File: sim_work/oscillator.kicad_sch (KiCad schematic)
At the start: 26 parts, among them U1 LM4562, U2 LM4562, U3 LM4562

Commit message: Oscillator schematic fixes, SimGUI verification, pipeline improvement plan
- Fix diode orientation (rotation 90/270 → 0/180) for correct pin-to-wire connectivity
- Fix feedback/VEE wire overlap that shorted -15V to inverting inputs
- Fix SPI0_CLK/VCTRL net collision (label → text annotation)
- Reduce feedback height above op-amps (fb_vert 14→6, damp_vert 22→10)
- Scale stroke widths in scale_schematic() for visibility at 3x
- Increase left margin (c1x 10→15) to prevent title clipping
- Add multi-point oscillator simulation results (D=12,60,605,1211,2421)
- Rewrite README with full project description and resource table
- Update PROJECT.md with Session 16-17 fixes and pipeline improvement roadmap

Co-Authored-By: Claude Opus 4.6 <noreply@anthropic.com>
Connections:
- net -15V: no longer C1.1, C2.1, R4.2, R5.1, R6.2, R7.1, U2.2 (-), U3.2 (-)
- net BP: now also C1.1, D1.1 (K), D1.2 (A), D2.1 (K), D2.2 (A), R4.2, R5.1, U2.2 (-)
- net LP: now also C2.1, D3.1 (K), D3.2 (A), D4.1 (K), D4.2 (A), R6.2, R7.1, U3.2 (-)
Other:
- note added: "1/5 attenuator Vin/5 to AD636"
- note added: "SPI0 -> DAC7800 controls VCTRL"
- note added: "STARTUP KICK + POWER SUPPLY"
- note added: "Startup Kick PULSE 0.1V 10us"
- note removed: "1/5 atten Vin/5 to AD636"
- note removed: "3.3V"
- note removed: "DAC_CS"
- note removed: "POWER SUPPLY"
- note removed: "PULSE 0.1V 10us"
- note removed: "SPI0 -> DAC7800 controls frequency"
- note removed: "SPI0_CLK"
- note removed: "SPI0_MOSI"
- note removed: "Startup Kick"
- note removed: "UART_TX"
- company: CircuitForge -> CircuitForge - Bob Smith

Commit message: Verification system overhaul + professional schematic layout
- Dynamic pin parser reads 22,607 KiCad symbol libraries for ALL component types
- Wire overlap detection catches collinear segments sharing ranges
- Wire merge post-processing auto-deduplicates overlapping wires
- simulate() now fails on non-zero exit codes, snapshots stale files
- Switched to 1x scale on standard A3/A4 paper (was 3x on custom paper)
- Section titles repositioned above components, MCU block boxed
- Clearance parameters added as kwargs for correction loop tuning

Oscillator: A3 1:1, 97% fill, 0 errors, 0 wire overlaps
TIA: A4 1:1, 96% fill, 0 errors, 0 wire overlaps

Co-Authored-By: Claude Opus 4.6 <noreply@anthropic.com>
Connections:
- net BP: no longer C1.1, D1.1 (K), D1.2 (A), D2.1 (K), D2.2 (A), R4.2, R5.1, U2.2 (-)
- net LP: no longer C2.1, D3.1 (K), D3.2 (A), D4.1 (K), D4.2 (A), R6.2, R7.1, U3.2 (-)
- net at R1.2, R2.2, U1.2 (-): no longer R3.1
- new net: D1.1 (K), D2.1 (K)
- new net: C1.1, R4.2, R5.1
- new net: C2.1, R6.2, R7.1
- new net: D3.1 (K), D4.1 (K)

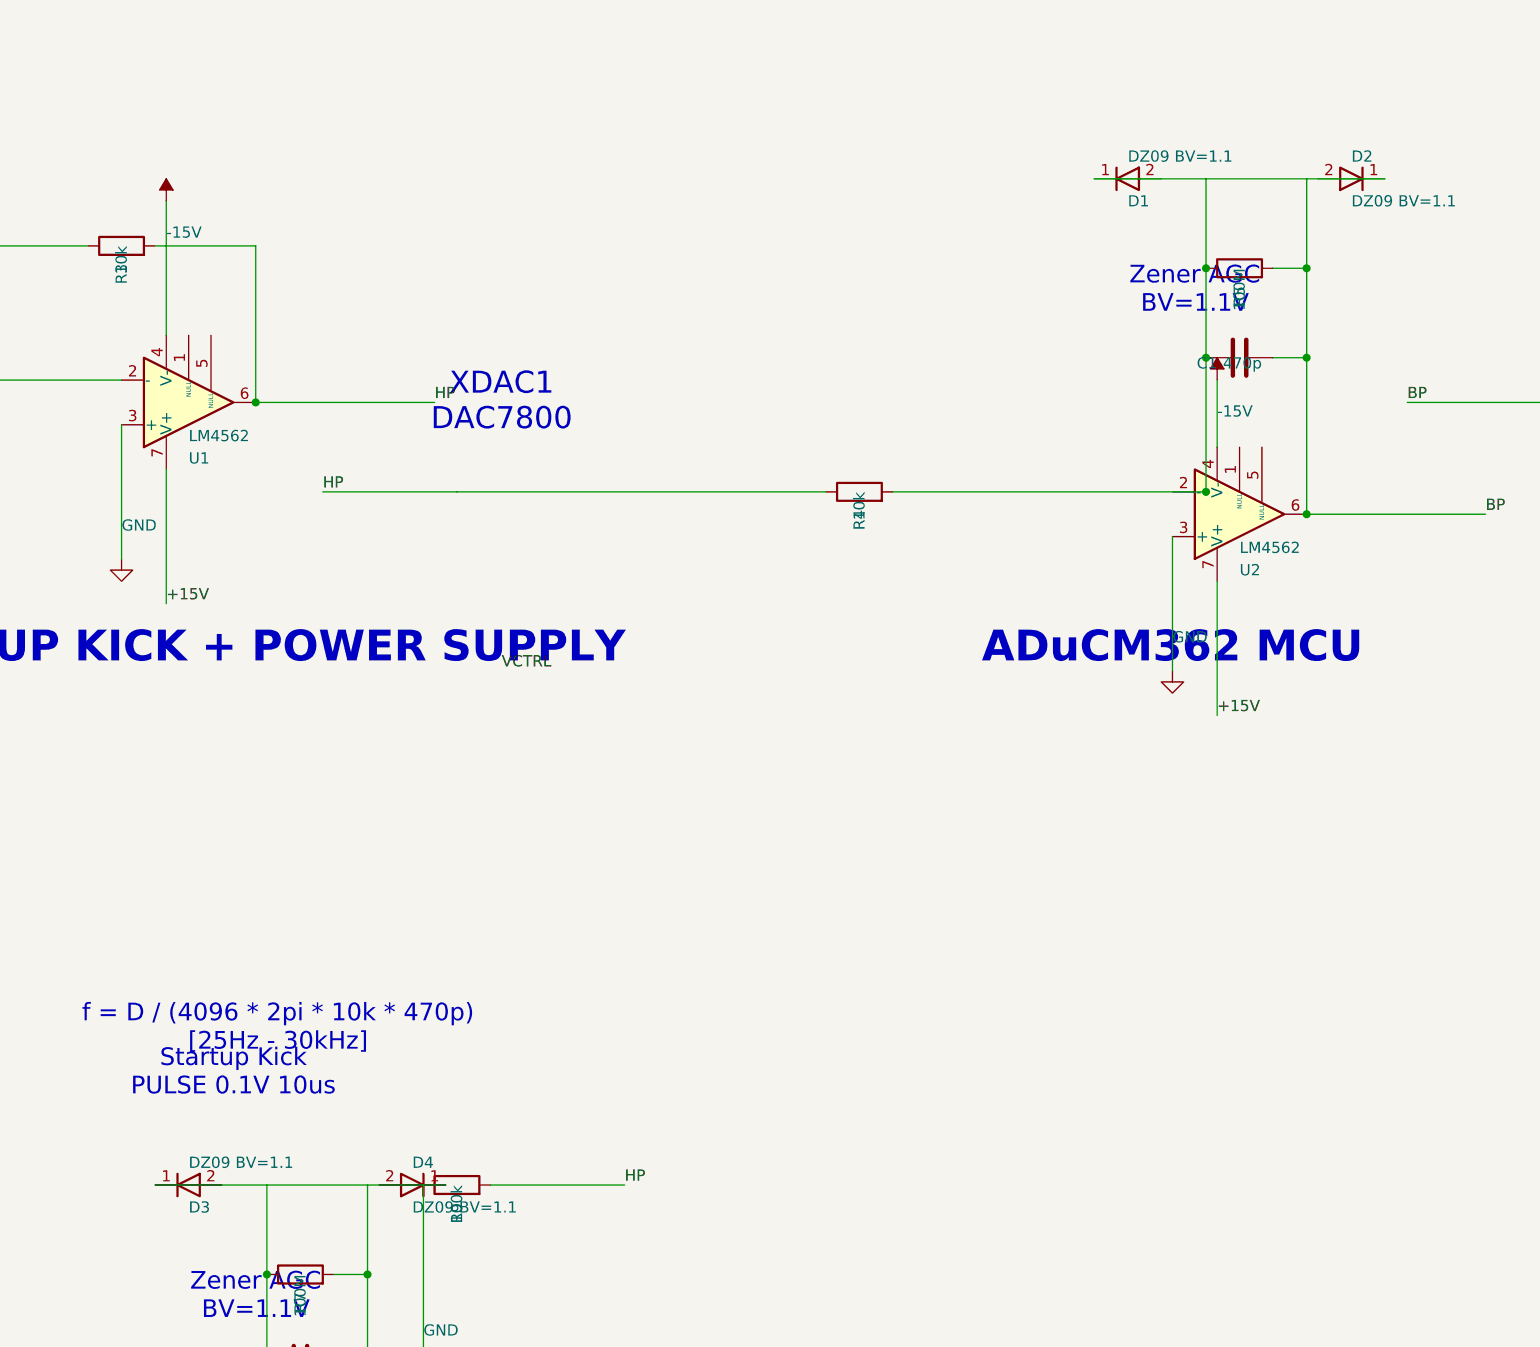
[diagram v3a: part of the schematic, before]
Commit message: Fix schematic connections, add docs and repo portability
- Input filters: R rotation=90 (horizontal), ESD diode rotations fixed,
  junction dots at cathode-signal connection, wires to GND symbols
- Relay ladder: flyback diode rotation 270->90 (K top, A bottom)
- Electrometer/Mux TIA: 4 junction dots each at T-junctions
- AD636 RMS detector: proper IC box with pin labels replaces text-only
- Oscillator blocks: D_Zener symbol, L-shaped cathode routing
- TIA blocks: title/function annotations on all 5 blocks
- New: requirements.txt, docs/oscillator_guide.md
- D_Zener.kicad_sym added to bundled symbols/
- .gitignore updated for docs/ and requirements.txt
- README updated with pip install -r requirements.txt
- PROJECT.md session 9 changelog
- SimGUI builds clean (0 errors)

Co-Authored-By: Claude Opus 4.6 <noreply@anthropic.com>
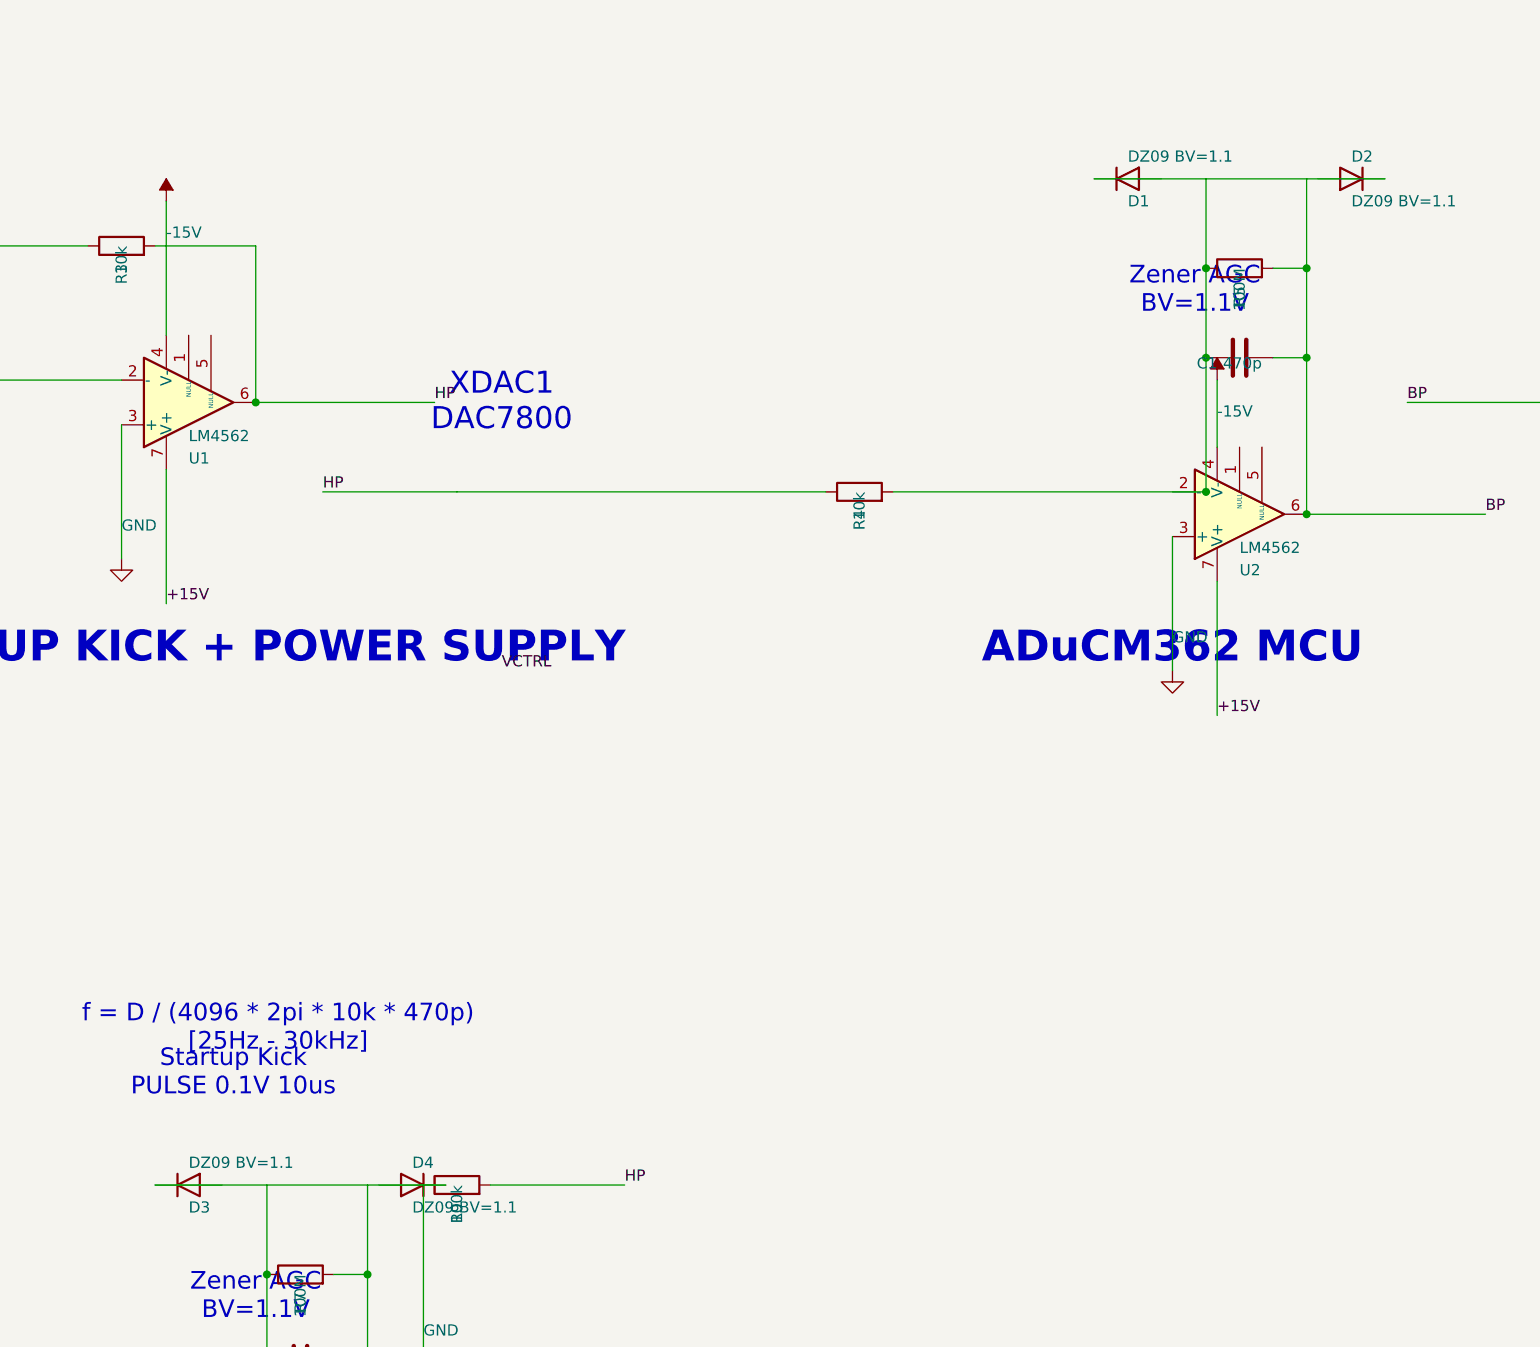
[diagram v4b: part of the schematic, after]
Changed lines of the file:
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@@
 		(instances
 			(project "State Variable Oscillator with MDAC Control"
-				(path "/075f6cc2-500d-4818-87f7-12acd1047ab1"
+				(path "/de47d635-bb16-490a-9463-fbb7ddc35300"
 					(reference "U1")
 					(unit 1)
@@
 		(instances
 			(project "State Variable Oscillator with MDAC Control"
-				(path "/075f6cc2-500d-4818-87f7-12acd1047ab1"
+				(path "/de47d635-bb16-490a-9463-fbb7ddc35300"
 					(reference "R1")
 					(unit 1)
@@
 		(instances
 			(project "State Variable Oscillator with MDAC Control"
-				(path "/075f6cc2-500d-4818-87f7-12acd1047ab1"
+				(path "/de47d635-bb16-490a-9463-fbb7ddc35300"
 					(reference "R2")
 					(unit 1)
@@
 		(instances
 			(project "State Variable Oscillator with MDAC Control"
-				(path "/075f6cc2-500d-4818-87f7-12acd1047ab1"
+				(path "/de47d635-bb16-490a-9463-fbb7ddc35300"
 					(reference "R3")
 					(unit 1)
@@
 		(instances
 			(project "State Variable Oscillator with MDAC Control"
-				(path "/075f6cc2-500d-4818-87f7-12acd1047ab1"
+				(path "/de47d635-bb16-490a-9463-fbb7ddc35300"
 					(reference "#PWR001")
 					(unit 1)
@@
 		(instances
 			(project "State Variable Oscillator with MDAC Control"
-				(path "/075f6cc2-500d-4818-87f7-12acd1047ab1"
+				(path "/de47d635-bb16-490a-9463-fbb7ddc35300"
 					(reference "#PWR002")
 					(unit 1)
@@
 		(instances
 			(project "State Variable Oscillator with MDAC Control"
-				(path "/075f6cc2-500d-4818-87f7-12acd1047ab1"
+				(path "/de47d635-bb16-490a-9463-fbb7ddc35300"
 					(reference "U2")
 					(unit 1)
@@
 		(instances
 			(project "State Variable Oscillator with MDAC Control"
-				(path "/075f6cc2-500d-4818-87f7-12acd1047ab1"
+				(path "/de47d635-bb16-490a-9463-fbb7ddc35300"
 					(reference "R4")
 					(unit 1)
@@
 		(instances
 			(project "State Variable Oscillator with MDAC Control"
-				(path "/075f6cc2-500d-4818-87f7-12acd1047ab1"
+				(path "/de47d635-bb16-490a-9463-fbb7ddc35300"
 					(reference "C1")
 					(unit 1)
@@
 		(instances
 			(project "State Variable Oscillator with MDAC Control"
-				(path "/075f6cc2-500d-4818-87f7-12acd1047ab1"
+				(path "/de47d635-bb16-490a-9463-fbb7ddc35300"
 					(reference "R5")
 					(unit 1)
@@
 		(instances
 			(project "State Variable Oscillator with MDAC Control"
-				(path "/075f6cc2-500d-4818-87f7-12acd1047ab1"
+				(path "/de47d635-bb16-490a-9463-fbb7ddc35300"
 					(reference "D1")
 					(unit 1)
@@
 		(instances
 			(project "State Variable Oscillator with MDAC Control"
-				(path "/075f6cc2-500d-4818-87f7-12acd1047ab1"
+				(path "/de47d635-bb16-490a-9463-fbb7ddc35300"
 					(reference "D2")
 					(unit 1)
@@
 		(instances
 			(project "State Variable Oscillator with MDAC Control"
-				(path "/075f6cc2-500d-4818-87f7-12acd1047ab1"
+				(path "/de47d635-bb16-490a-9463-fbb7ddc35300"
 					(reference "#PWR003")
 					(unit 1)
@@
 		(instances
 			(project "State Variable Oscillator with MDAC Control"
-				(path "/075f6cc2-500d-4818-87f7-12acd1047ab1"
+				(path "/de47d635-bb16-490a-9463-fbb7ddc35300"
 					(reference "#PWR004")
 					(unit 1)
@@
 		(instances
 			(project "State Variable Oscillator with MDAC Control"
-				(path "/075f6cc2-500d-4818-87f7-12acd1047ab1"
+				(path "/de47d635-bb16-490a-9463-fbb7ddc35300"
 					(reference "R10")
 					(unit 1)
@@
 		(instances
 			(project "State Variable Oscillator with MDAC Control"
-				(path "/075f6cc2-500d-4818-87f7-12acd1047ab1"
+				(path "/de47d635-bb16-490a-9463-fbb7ddc35300"
 					(reference "R11")
 					(unit 1)
@@
 		(instances
 			(project "State Variable Oscillator with MDAC Control"
-				(path "/075f6cc2-500d-4818-87f7-12acd1047ab1"
+				(path "/de47d635-bb16-490a-9463-fbb7ddc35300"
 					(reference "#PWR005")
 					(unit 1)
@@
 		(instances
 			(project "State Variable Oscillator with MDAC Control"
-				(path "/075f6cc2-500d-4818-87f7-12acd1047ab1"
+				(path "/de47d635-bb16-490a-9463-fbb7ddc35300"
 					(reference "C3")
 					(unit 1)
@@
 		(instances
 			(project "State Variable Oscillator with MDAC Control"
-				(path "/075f6cc2-500d-4818-87f7-12acd1047ab1"
+				(path "/de47d635-bb16-490a-9463-fbb7ddc35300"
 					(reference "#PWR006")
 					(unit 1)
@@
 		(instances
 			(project "State Variable Oscillator with MDAC Control"
-				(path "/075f6cc2-500d-4818-87f7-12acd1047ab1"
+				(path "/de47d635-bb16-490a-9463-fbb7ddc35300"
 					(reference "U3")
 					(unit 1)
@@
 		(instances
 			(project "State Variable Oscillator with MDAC Control"
-				(path "/075f6cc2-500d-4818-87f7-12acd1047ab1"
+				(path "/de47d635-bb16-490a-9463-fbb7ddc35300"
 					(reference "R6")
 					(unit 1)
@@
 		(instances
 			(project "State Variable Oscillator with MDAC Control"
-				(path "/075f6cc2-500d-4818-87f7-12acd1047ab1"
+				(path "/de47d635-bb16-490a-9463-fbb7ddc35300"
 					(reference "C2")
 					(unit 1)
@@
 		(instances
 			(project "State Variable Oscillator with MDAC Control"
-				(path "/075f6cc2-500d-4818-87f7-12acd1047ab1"
+				(path "/de47d635-bb16-490a-9463-fbb7ddc35300"
 					(reference "R7")
 					(unit 1)
@@
 		(instances
 			(project "State Variable Oscillator with MDAC Control"
-				(path "/075f6cc2-500d-4818-87f7-12acd1047ab1"
+				(path "/de47d635-bb16-490a-9463-fbb7ddc35300"
 					(reference "D3")
 					(unit 1)
@@
 		(instances
 			(project "State Variable Oscillator with MDAC Control"
-				(path "/075f6cc2-500d-4818-87f7-12acd1047ab1"
+				(path "/de47d635-bb16-490a-9463-fbb7ddc35300"
 					(reference "D4")
 					(unit 1)
@@
 		(instances
 			(project "State Variable Oscillator with MDAC Control"
-				(path "/075f6cc2-500d-4818-87f7-12acd1047ab1"
+				(path "/de47d635-bb16-490a-9463-fbb7ddc35300"
 					(reference "#PWR007")
 					(unit 1)
@@
 		(instances
 			(project "State Variable Oscillator with MDAC Control"
-				(path "/075f6cc2-500d-4818-87f7-12acd1047ab1"
+				(path "/de47d635-bb16-490a-9463-fbb7ddc35300"
 					(reference "#PWR008")
 					(unit 1)
@@
 		(instances
 			(project "State Variable Oscillator with MDAC Control"
-				(path "/075f6cc2-500d-4818-87f7-12acd1047ab1"
+				(path "/de47d635-bb16-490a-9463-fbb7ddc35300"
 					(reference "R8")
 					(unit 1)
@@
 		(instances
 			(project "State Variable Oscillator with MDAC Control"
-				(path "/075f6cc2-500d-4818-87f7-12acd1047ab1"
+				(path "/de47d635-bb16-490a-9463-fbb7ddc35300"
 					(reference "#PWR009")
 					(unit 1)
@@
 		(instances
 			(project "State Variable Oscillator with MDAC Control"
-				(path "/075f6cc2-500d-4818-87f7-12acd1047ab1"
+				(path "/de47d635-bb16-490a-9463-fbb7ddc35300"
 					(reference "R9")
 					(unit 1)
@@
 		(instances
 			(project "State Variable Oscillator with MDAC Control"
-				(path "/075f6cc2-500d-4818-87f7-12acd1047ab1"
+				(path "/de47d635-bb16-490a-9463-fbb7ddc35300"
 					(reference "#PWR010")
 					(unit 1)
@@
 		(instances
 			(project "State Variable Oscillator with MDAC Control"
-				(path "/075f6cc2-500d-4818-87f7-12acd1047ab1"
+				(path "/de47d635-bb16-490a-9463-fbb7ddc35300"
 					(reference "C6")
 					(unit 1)
@@
 		(instances
 			(project "State Variable Oscillator with MDAC Control"
-				(path "/075f6cc2-500d-4818-87f7-12acd1047ab1"
+				(path "/de47d635-bb16-490a-9463-fbb7ddc35300"
 					(reference "#PWR011")
 					(unit 1)
@@
 		(instances
 			(project "State Variable Oscillator with MDAC Control"
-				(path "/075f6cc2-500d-4818-87f7-12acd1047ab1"
+				(path "/de47d635-bb16-490a-9463-fbb7ddc35300"
 					(reference "#PWR012")
 					(unit 1)
@@
 		(instances
 			(project "State Variable Oscillator with MDAC Control"
-				(path "/075f6cc2-500d-4818-87f7-12acd1047ab1"
+				(path "/de47d635-bb16-490a-9463-fbb7ddc35300"
 					(reference "C7")
 					(unit 1)
@@
 		(instances
 			(project "State Variable Oscillator with MDAC Control"
-				(path "/075f6cc2-500d-4818-87f7-12acd1047ab1"
+				(path "/de47d635-bb16-490a-9463-fbb7ddc35300"
 					(reference "#PWR013")
 					(unit 1)
@@
 		(instances
 			(project "State Variable Oscillator with MDAC Control"
-				(path "/075f6cc2-500d-4818-87f7-12acd1047ab1"
+				(path "/de47d635-bb16-490a-9463-fbb7ddc35300"
 					(reference "C8")
 					(unit 1)
@@
 		(instances
 			(project "State Variable Oscillator with MDAC Control"
-				(path "/075f6cc2-500d-4818-87f7-12acd1047ab1"
+				(path "/de47d635-bb16-490a-9463-fbb7ddc35300"
 					(reference "#PWR014")
 					(unit 1)
@@
 		(instances
 			(project "State Variable Oscillator with MDAC Control"
-				(path "/075f6cc2-500d-4818-87f7-12acd1047ab1"
+				(path "/de47d635-bb16-490a-9463-fbb7ddc35300"
 					(reference "#PWR015")
 					(unit 1)
@@
 		(instances
 			(project "State Variable Oscillator with MDAC Control"
-				(path "/075f6cc2-500d-4818-87f7-12acd1047ab1"
+				(path "/de47d635-bb16-490a-9463-fbb7ddc35300"
 					(reference "C4")
 					(unit 1)
@@
 		(instances
 			(project "State Variable Oscillator with MDAC Control"
-				(path "/075f6cc2-500d-4818-87f7-12acd1047ab1"
+				(path "/de47d635-bb16-490a-9463-fbb7ddc35300"
 					(reference "#PWR016")
 					(unit 1)
@@
 		(instances
 			(project "State Variable Oscillator with MDAC Control"
-				(path "/075f6cc2-500d-4818-87f7-12acd1047ab1"
+				(path "/de47d635-bb16-490a-9463-fbb7ddc35300"
 					(reference "C5")
 					(unit 1)
@@
 		(instances
 			(project "State Variable Oscillator with MDAC Control"
-				(path "/075f6cc2-500d-4818-87f7-12acd1047ab1"
+				(path "/de47d635-bb16-490a-9463-fbb7ddc35300"
 					(reference "#PWR017")
 					(unit 1)

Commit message: Add comparison mode, fix SimGUI subprocess popups, DAC7800 IC boxes
- SimGUI: fix Python path detection (FindPython searches Python312/313/311)
- SimGUI: suppress console popup windows (CREATE_NO_WINDOW for subprocess)
- SimGUI: add Comparison project (MDAC vs Analog oscillator side-by-side)
- SimGUI: fix async wrapping (direct await instead of Task.Run)
- Pipeline: draw DAC7800 as proper IC box with pin labels (VREF/IOUT/VCTRL)
- Pipeline: fix electrometer_362 layout (spacing, junction dots at T-junctions)
- Pipeline: fix summing amp gain annotations (BP=-0.455, not -2.2)
- Pipeline: add analog_osc command for friend's SVF oscillator simulation
- Docs: comparison_guide.md, updated README and PROJECT tracker

Co-Authored-By: Claude Opus 4.6 <noreply@anthropic.com>
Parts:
- removed D1, D2, D3, D4: DZ09 BV=1.1, symbol D:D
- added D1, D2, D3, D4: DZ09 BV=1.1, symbol D_Zener:D_Zener
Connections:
- net +15V: now also U1.4 (V-), U2.4 (V-), U3.4 (V-); no longer U1.7 (V+), U2.7 (V+), U3.7 (V+)
- net -15V: now also U1.7 (V+), U2.7 (V+), U3.7 (V+); no longer U1.4 (V-), U2.4 (V-), U3.4 (V-)
- net BP: now also D2.1 (K); no longer R6.1
- net GND: now also U1.2 (-), U2.2 (-), U3.2 (-); no longer U1.3 (+), U2.3 (+), U3.3 (+)
- net HP: no longer R4.1
- net LP: now also D4.1 (K)
- net at C1.1, R4.2, R5.1: now also D1.1 (K)
- net at R1.2, R2.2: now also U1.3 (+); no longer U1.2 (-)
- net at C2.1, R6.2, R7.1: now also D3.1 (K)
- new net: D3.2 (A), D4.2 (A)
- new net: D1.2 (A), D2.2 (A)
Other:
- note added: "IOUT"
- note added: "VCTRL"
- note added: "VREF"
